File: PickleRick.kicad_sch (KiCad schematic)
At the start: 83 parts, among them J1 Conn_01x06_Male, J10 Conn_01x03_Male, J11 Conn_01x02_Male, J2 Conn_01x02_Male, J3 Conn_01x02_Male, J4 Micro_SD_Card_Det, J5 292227-7, Q1 MMDT2222A, Q2 PMV20ENR, U1 SN65HVD230, U2 ESP32-WROOM-32D, U3 MS5607-02BA

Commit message: working on v2
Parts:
- removed C1, C2, C3: 0.1uF, Capacitor_SMD:C_0603_1608Metric, symbol Device:C_Small
- removed C27: 160pF, Capacitor_SMD:C_0603_1608Metric, symbol Device:C_Small
- removed C28, C5: 100nF, Capacitor_SMD:C_0603_1608Metric, symbol Device:C_Small
- removed C36: 10uF, Capacitor_SMD:C_0603_1608Metric, symbol Device:C_Small
- removed C37: 0.1uF, Capacitor_SMD:C_0603_1608Metric, symbol Device:C
- removed C38: 220pF, Capacitor_SMD:C_0603_1608Metric, symbol Device:C_Small
- removed C39: 220 pF, Capacitor_SMD:C_0603_1608Metric, symbol Device:C_Small
- removed C4: 10uf, Capacitor_SMD:C_0603_1608Metric, symbol Device:C_Small
- removed D19: SM712_SOT23, Package_TO_SOT_SMD:SOT-23, symbol Diode:SM712_SOT23
- removed J10: Conn_01x03_Male, Connector_PinHeader_2.54mm:PinHeader_1x03_P2.54mm_Vertical, symbol Connector:Conn_01x03_Male
- removed J2, J3: Conn_01x02_Male, Connector_PinHeader_2.54mm:PinHeader_1x02_P2.54mm_Vertical, symbol Connector:Conn_01x02_Male
- removed JP1: SolderJumper_2_Open, Jumper:SolderJumper-2_P1.3mm_Open_RoundedPad1.0x1.5mm, symbol Jumper:SolderJumper_2_Open
- removed Q1: MMDT2222A, Package_TO_SOT_SMD:SOT-363_SC-70-6, symbol Transistor_BJT:MMDT2222A
- removed R1, R14, R15, R16, R17, R18, R19, R2, R20, R3, R5: 10K, Resistor_SMD:R_0603_1608Metric, symbol Device:R_Small
- removed R12, R13: 4.7K, Resistor_SMD:R_0603_1608Metric, symbol Device:R_Small
- removed R39, R40: 90, Resistor_SMD:R_0603_1608Metric, symbol Device:R_Small
- removed R4, R6: 470, Resistor_SMD:R_0603_1608Metric, symbol Device:R_Small
- removed R41: 10k, Resistor_SMD:R_0603_1608Metric, symbol Device:R_Small
- removed R48, R49: 60, Resistor_SMD:R_0603_1608Metric, symbol Device:R
- removed TP1, TP11, TP12, TP13, TP14, TP15, TP16, TP17, TP18, TP19, TP2, TP20, TP21, TP22, TP23, TP24, TP25, TP26, TP3, TP6, TP8: TestPoint, TestPoint:TestPoint_Pad_D1.0mm, symbol Connector:TestPoint
- removed U1: SN65HVD230, Package_SO:SOIC-8_3.9x4.9mm_P1.27mm, symbol Interface_CAN_LIN:SN65HVD230
- removed U2: ESP32-WROOM-32D, RF_Module:ESP32-WROOM-32, symbol RF_Module:ESP32-WROOM-32
- added 12VLED?: 12V_LED, Resistor_SMD:R_0402_1005Metric, symbol Device:LED_Small
- added BOOTJUMPER?, ENJUMPER?: Conn_01x02_Male, Connector_PinHeader_2.54mm:PinHeader_1x02_P2.54mm_Vertical, symbol Connector:Conn_01x02_Male
- added C? (x3): 1uF, Capacitor_SMD:C_0402_1005Metric, symbol Device:C_Small
- added C? (x6): 0.1uF, Capacitor_SMD:C_0402_1005Metric, symbol Device:C_Small
- added C?: 4.2pF, Capacitor_SMD:C_0402_1005Metric, symbol Device:C_Small
- added C?: 10nF, Capacitor_SMD:C_0402_1005Metric, symbol Device:C_Small
- added C? (x2): C, Capacitor_SMD:C_0402_1005Metric, symbol Device:C_Small
- added C?: 10uF, Capacitor_SMD:C_0402_1005Metric, symbol Device:C_Small
- added L?: 2.0nH, Inductor_SMD:L_0402_1005Metric, symbol Device:L
- added L?: 20nH, Inductor_SMD:L_0402_1005Metric, symbol Device:L
- added R?: 47.5, Resistor_SMD:R_0402_1005Metric, symbol Device:R_Small
- added R? (x2): 10K, Resistor_SMD:R_0402_1005Metric, symbol Device:R_Small
- added R?: 499, Resistor_SMD:R_0402_1005Metric, symbol Device:R_Small
- added R?: 3k, Resistor_SMD:R_0402_1005Metric, symbol Device:R_Small
- added U?: ESP32-S3, Package_DFN_QFN:QFN-56-1EP_7x7mm_P0.4mm_EP5.6x5.6mm, symbol Espressif:ESP32-S3
- added Y?: 40MHz±10ppm, Crystal:Crystal_SMD_2016-4Pin_2.0x1.6mm, symbol Device:Crystal_GND24
- J1: value Conn_01x06_Male -> RBUS
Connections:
- net +3V3: now also C?.1, C?.1, C?.1, C?.1, C?.1, C?.1, C?.1, L?.1, R?.1, R?.1, U?.20 (VDD3P3_RTC), U?.46 (VDD3P3_CPU), U?.55 (VDDA), U?.56 (VDDA)
- net BOOT: now also BOOTJUMPER?.1 (Pin_1), C?.1, R?.2, U?.5 (GPIO0/BOOT)
- net GND: now also 12VLED?.1 (K), BOOTJUMPER?.2 (Pin_2), C?.2, C?.2, C?.2, C?.2, C?.2, C?.2, C?.2, C?.2, C?.2, C?.2, C?.2, C?.2, C?.2, ENJUMPER?.2 (Pin_2), R?.1, U?.57 (GND), Y?.2, Y?.4
- net TXD: now also R?.1
- net CAN_HIGH renamed CAN+
- net CAN_LOW renamed CAN-
- new net: C?.1, L?.2, U?.2 (VDD3P3), U?.3 (VDD3P3)
- new net: C?.1, R?.2
- new net: C?.2, U?.1 (LNA_IN/RF)
- new net: R?.2, U?.49 (U0TXD/PROG/GPIO43)
- new net: C?.1, U?.53 (XTAL_N), Y?.3
- new net: L?.1, U?.54 (XTAL_P)
- new net: C?.1, L?.2, Y?.1
- new net: 12VLED?.2 (A), R?.2
- new net +12V: R?.1
- new net CHIP_PU: C?.1, C?.1, ENJUMPER?.1 (Pin_1), R?.2, U?.4 (CHIP_PU/RESET)
- new net Data+: U?.26 (GPIO20/USB_D+/ADC2_CH9)
- new net Data-: U?.25 (GPIO19/USB_D-/ADC2_CH8)
- no-connect marks 8 -> 11
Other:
- removed sheet usb_uart
- added sheet CAN-BUS (can.kicad_sch)
- added sheet USB -> UART (usb-uart.kicad_sch)
- note added: "CAN + is CAN High CAN - is CAN LOW Named with a + and - as it is a KiCad requirement to route differential tracks"
- note added: "Controls JTAG source, don't use"
- note added: "Controls bootmode, don't use."
- note added: "TBD C and R value to get a total series impedance of 50 ohms at 2.4GHz"
- moved on the sheet: D1, D2, D3, D4, D5, J1, R10, R11, R7, R8, R9, TP27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

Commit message: v2 time
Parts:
- removed D6: D_Schottky, Diode_SMD:D_SOD-123F, symbol Device:D_Schottky
- added R11: 1k, Resistor_SMD:R_0402_1005Metric, symbol Device:R_Small
- added TP1, TP2, TP3, TP4: TestPoint, TestPoint:TestPoint_Pad_D1.0mm, symbol Connector:TestPoint
- C15: renamed from C6; footprint Capacitor_SMD:C_0603_1608Metric -> Capacitor_SMD:C_0402_1005Metric
- C16: renamed from C23; footprint Capacitor_SMD:C_0603_1608Metric -> Capacitor_SMD:C_0402_1005Metric
- D1, D2, D3, D4, D5: footprint LED_SMD:LED_0603_1608Metric -> LED_SMD:LED_0402_1005Metric
- R10: renamed from R?; value 3k -> 5k; footprint Resistor_SMD:R_0402_1005Metric -> Resistor_SMD:R_0603_1608Metric
- R12: renamed from R21; footprint Resistor_SMD:R_0603_1608Metric -> Resistor_SMD:R_0402_1005Metric
- R13: renamed from R22; footprint Resistor_SMD:R_0603_1608Metric -> Resistor_SMD:R_0402_1005Metric
- R2: renamed from R7; footprint Resistor_SMD:R_0603_1608Metric -> Resistor_SMD:R_0402_1005Metric
- R3: renamed from R8; footprint Resistor_SMD:R_0603_1608Metric -> Resistor_SMD:R_0402_1005Metric
- R4: renamed from R9; footprint Resistor_SMD:R_0603_1608Metric -> Resistor_SMD:R_0402_1005Metric
- R5: renamed from R10; footprint Resistor_SMD:R_0603_1608Metric -> Resistor_SMD:R_0402_1005Metric
- R7: renamed from R11; footprint Resistor_SMD:R_0603_1608Metric -> Resistor_SMD:R_0402_1005Metric
- gave numbers to parts that had none: 25
- renumbered J11 to J2, J5 to J3, Q2 to Q1, TP27 to TP5, TP28 to TP6, U3 to U2
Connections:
- net +3V3: now also R11.1
- net BARO_CS: now also U1.12 (GPIO7/ADC1_CH6)
- net BattVolt: now also U1.7 (GPIO2/ADC1_CH1)
- net Buzzer: now also U1.6 (GPIO1/ADC1_CH0)
- net CAN_RX: now also U1.23 (GPIO17/ADC2_CH6/DAC_2)
- net CAN_TX: now also U1.24 (GPIO18/ADC2_CH7/DAC_1)
- net HSPI_MISO: now also U1.43 (GPIO38)
- net HSPI_MOSI: now also U1.42 (GPIO37)
- net HSPI_SCLK: now also U1.41 (GPIO36)
- net IMU1_CS: now also U1.11 (GPIO6/ADC1_CH5)
- net IMU2_CS: now also U1.10 (GPIO5/ADC1_CH4)
- net LORA_CS: now also U1.13 (GPIO8/ADC1_CH7)
- net LORA_INT: now also U1.15 (GPIO10/ADC1_CH9)
- net LORA_RESET: now also U1.14 (GPIO9/ADC1_CH8)
- net MAG_CS: now also U1.9 (GPIO4/ADC1_CH3)
- net RXD: now also U1.50 (U0RXD/PROG/GPIO44)
- net SCL: now also U1.28 (SPI_CS1/GPIO26)
- net SD1_CS: now also U1.19 (GPIO14/ADC2_CH3)
- net SD1_DET: now also U1.18 (GPIO13/ADC2_CH2)
- net SD2_CS: now also U1.17 (GPIO12/ADC2_CH1)
- net SD2_DET: now also U1.16 (GPIO11/ADC2_CH0)
- net SDA: now also U1.27 (GPIO21)
- net VSPI_MISO: now also U1.40 (GPIO35)
- net VSPI_MOSI: now also U1.38 (GPIO33)
- net VSPI_SCLK: now also U1.39 (GPIO34)
- net at J2.1 (Pin_1): now also Q1.3 (D), R11.2
- net JTAG_MTCK: now reaches U1.44 (MTCK/JTAG/GPIO39)
- net JTAG_MTCK: now also TP1.1
- net JTAG_MTDO: now reaches U1.45 (MTDO/JTAG/GPIO40)
- net JTAG_MTDO: now also TP2.1
- net JTAG_MTDI: now reaches U1.47 (MTDI/JTAG/GPIO41)
- net JTAG_MTDI: now also TP3.1
- net JTAG_MTMS: now reaches U1.48 (MTMS/JTAG/GPIO42)
- net JTAG_MTMS: now also TP4.1
- no-connect marks 11 -> 14
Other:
- moved on the sheet: C1, C5, J2, Q1

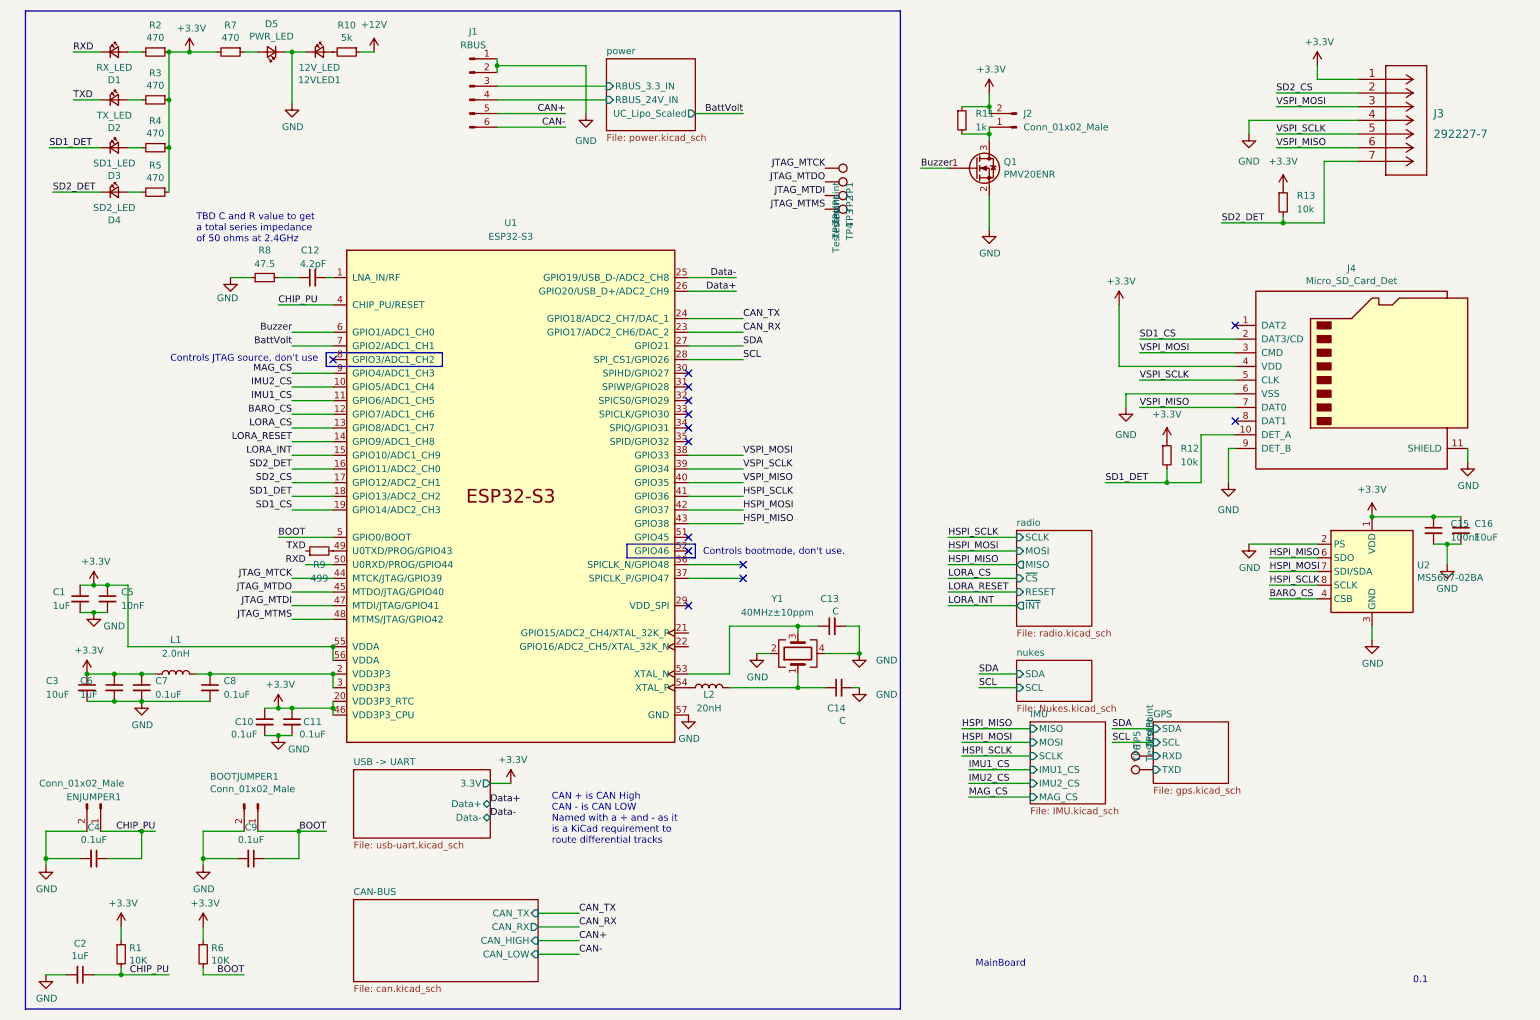
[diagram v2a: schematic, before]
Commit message: Conitnued with v2, NB pinout of external sd card has changed!!! Chest needs to be updated before manufacturing!!!
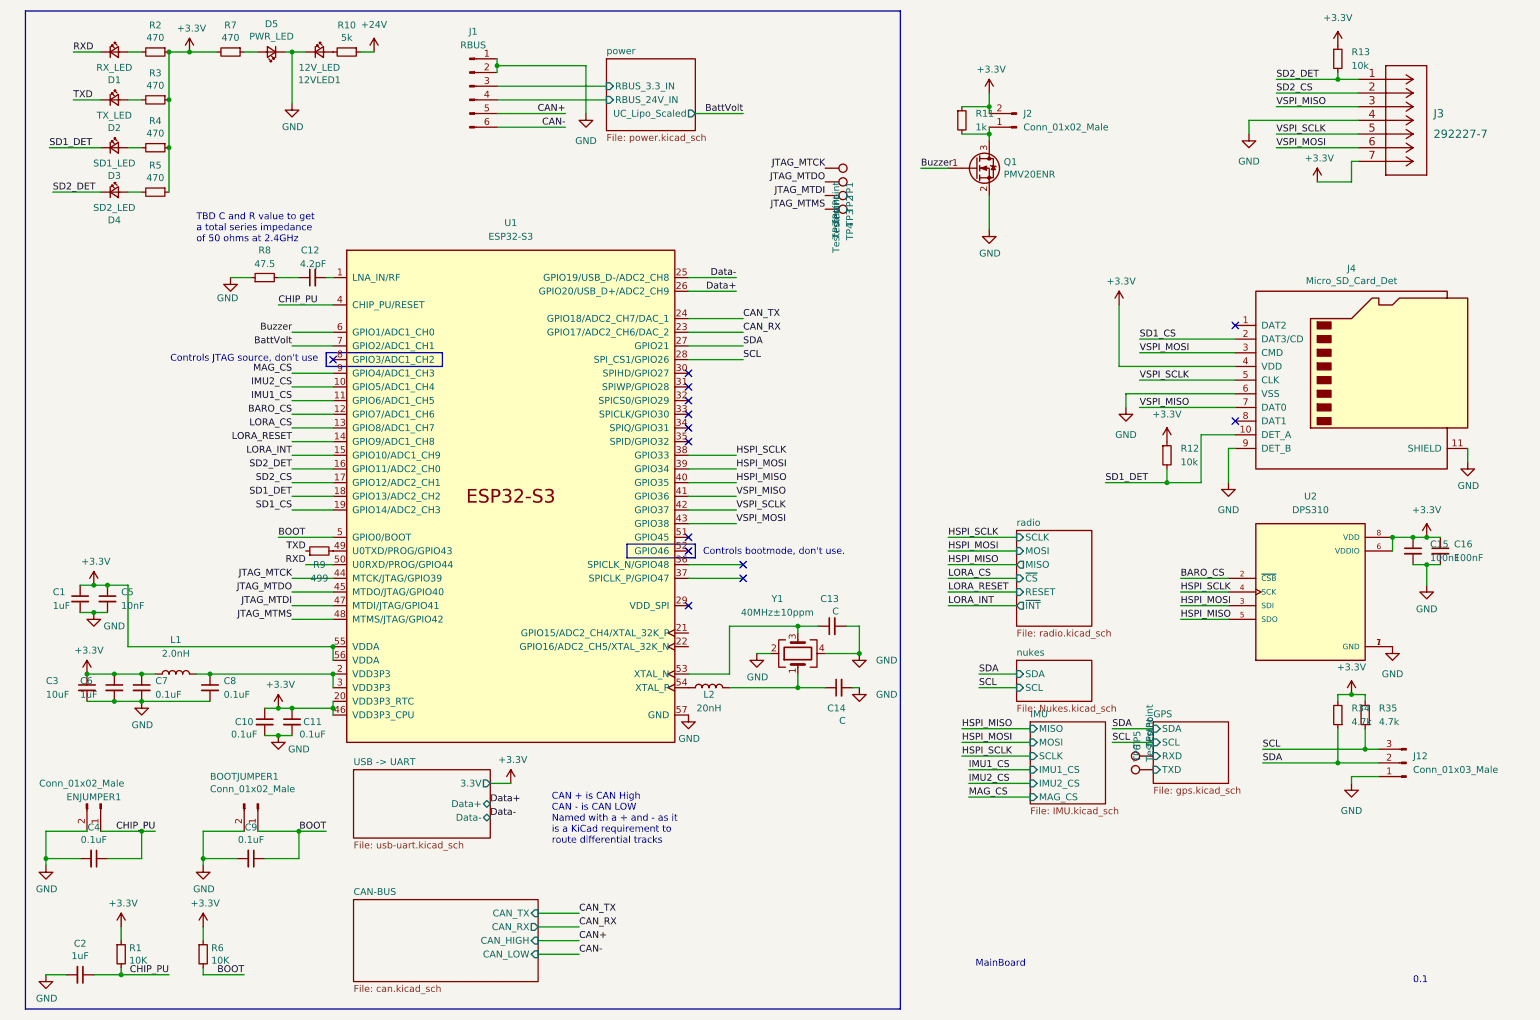
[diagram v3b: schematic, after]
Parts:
- removed U2: MS5607-02BA, Package_LGA:LGA-8_3x5mm_P1.25mm, symbol Sensor_Pressure:MS5607-02BA
- added J12: Conn_01x03_Male, Connector_PinHeader_2.54mm:PinHeader_1x03_P2.54mm_Vertical, symbol Connector:Conn_01x03_Male
- added R34, R35: 4.7k, symbol Device:R_Small
- added U2: DPS310, XDCR_DPS310, symbol iclr:DPS310
- C16: value 10uF -> 100nF
- U1: footprint Package_DFN_QFN:QFN-56-1EP_7x7mm_P0.4mm_EP5.6x5.6mm -> iclr:QFN40P700X700X90-57N
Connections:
- net +3V3: now also J3.7, R34.2, R35.2, U2.6 (VDDIO), U2.8 (VDD); no longer J3.1
- net BARO_CS: now also U2.2 (~{CSB})
- net GND: now also J12.1 (Pin_1), U2.1 (GND), U2.7 (GND)
- net HSPI_MISO: now also U1.40 (GPIO35), U2.5 (SDO); no longer U1.43 (GPIO38)
- net HSPI_MOSI: now also U1.39 (GPIO34), U2.3 (SDI); no longer U1.42 (GPIO37)
- net HSPI_SCLK: now also U1.38 (GPIO33), U2.4 (SCK); no longer U1.41 (GPIO36)
- net SCL: now also J12.3 (Pin_3), R35.1
- net SD2_DET: now also J3.1; no longer J3.7
- net SDA: now also J12.2 (Pin_2), R34.1
- net VSPI_MISO: now also J3.3, U1.41 (GPIO36); no longer J3.6, U1.40 (GPIO35)
- net VSPI_MOSI: now also J3.6, U1.43 (GPIO38); no longer J3.3, U1.38 (GPIO33)
- net VSPI_SCLK: now also U1.42 (GPIO37); no longer U1.39 (GPIO34)
- net +12V renamed +24V
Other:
- moved on the sheet: C15, C16, R13
